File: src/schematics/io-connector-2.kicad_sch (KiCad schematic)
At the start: 1 part, among them J13 DDR4_SODIMM_Board

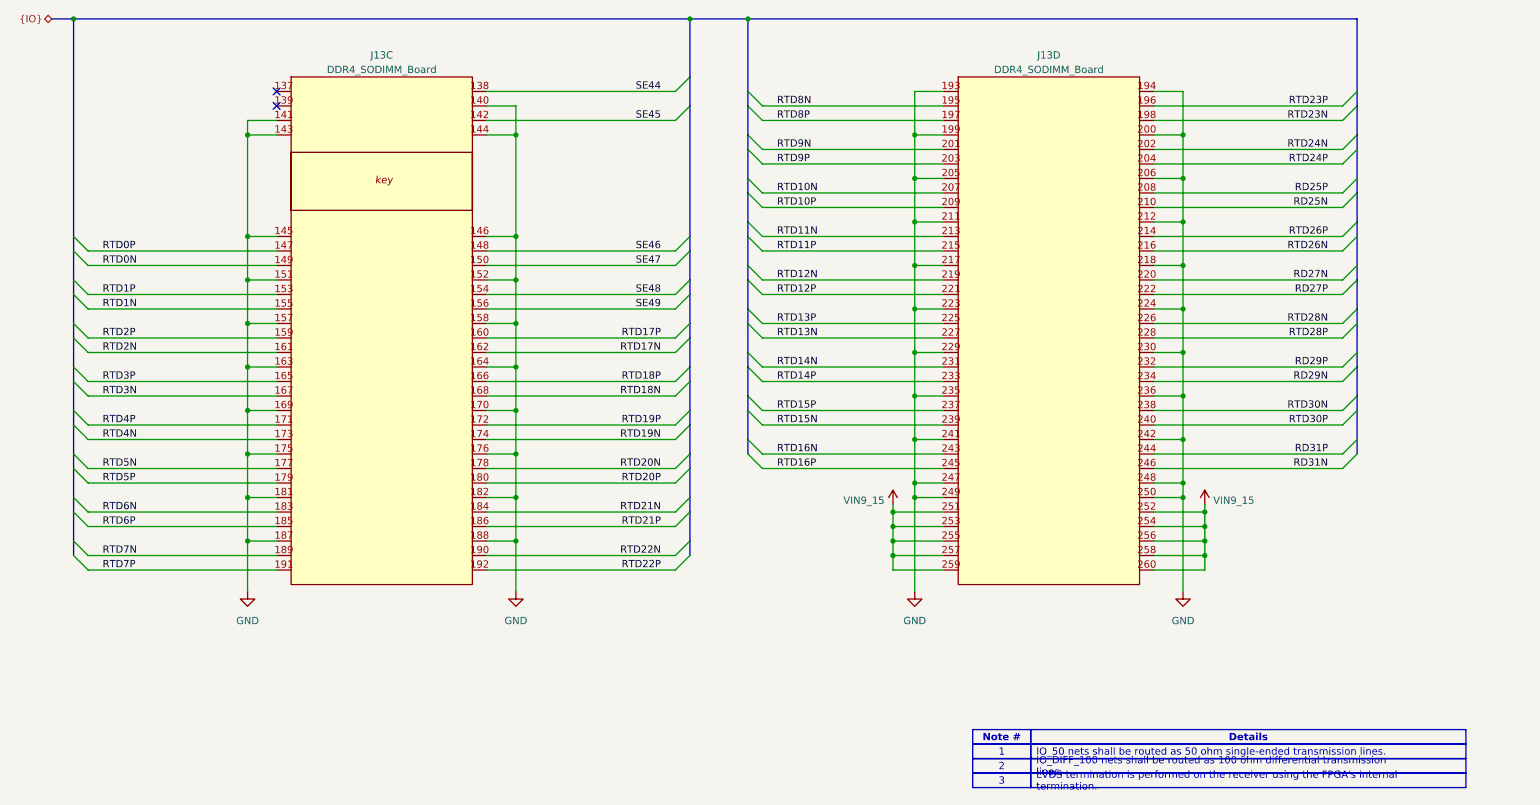
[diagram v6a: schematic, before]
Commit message: Fix diff pair skew
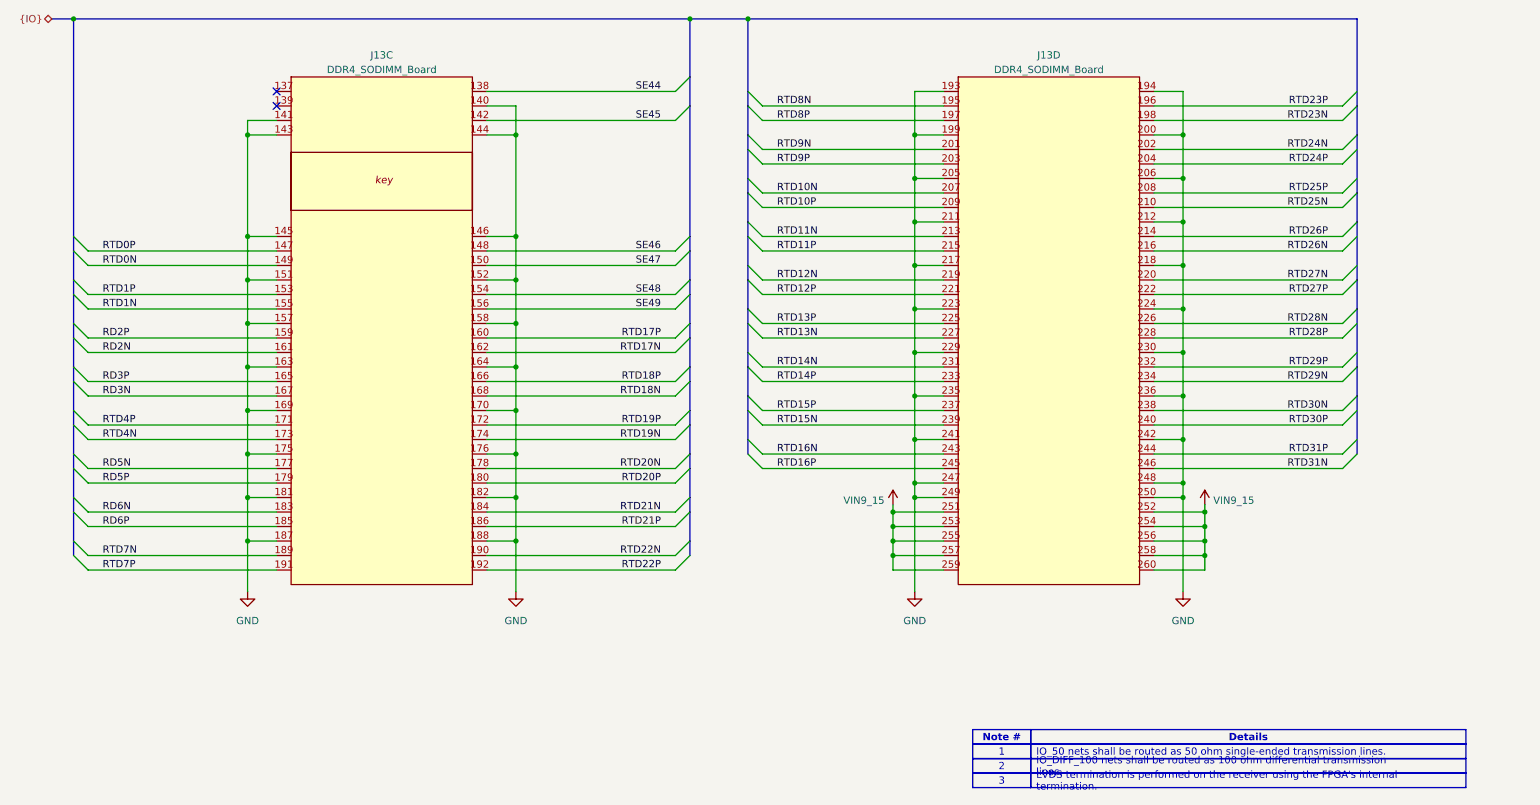
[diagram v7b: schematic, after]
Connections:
- net RD25N renamed RTD25N
- net RD25P renamed RTD25P
- net RD27N renamed RTD27N
- net RD27P renamed RTD27P
- net RD29N renamed RTD29N
- net RD29P renamed RTD29P
- net RD31N renamed RTD31N
- net RD31P renamed RTD31P
- net RTD2N renamed RD2N
- net RTD2P renamed RD2P
- net RTD3N renamed RD3N
- net RTD3P renamed RD3P
- net RTD5N renamed RD5N
- net RTD5P renamed RD5P
- net RTD6N renamed RD6N
- net RTD6P renamed RD6P
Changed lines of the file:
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@@
 		)
 	)
-	(label "RD27P"
+	(label "RTD27P"
 		(at 257.81 86.36 180)
 		(effects
@@
 		)
 	)
-	(label "RTD3P"
+	(label "RD3P"
 		(at 43.18 101.6 0)
 		(effects
@@
 		)
 	)
-	(label "RTD2P"
+	(label "RD2P"
 		(at 43.18 93.98 0)
 		(effects
@@
 		)
 	)
-	(label "RTD6P"
+	(label "RD6P"
 		(at 43.18 127 0)
 		(effects
@@
 		)
 	)
-	(label "RTD5N"
+	(label "RD5N"
 		(at 43.18 116.84 0)
 		(effects
@@
 		)
 	)
-	(label "RD29P"
+	(label "RTD29P"
 		(at 257.81 99.06 180)
 		(effects
@@
 		)
 	)
-	(label "RD29N"
+	(label "RTD29N"
 		(at 257.81 101.6 180)
 		(effects
@@
 		)
 	)
-	(label "RD31N"
+	(label "RTD31N"
 		(at 257.81 116.84 180)
 		(effects
@@
 		)
 	)
-	(label "RTD2N"
+	(label "RD2N"
 		(at 43.18 96.52 0)
 		(effects
@@
 		)
 	)
-	(label "RD25N"
+	(label "RTD25N"
 		(at 257.81 71.12 180)
 		(effects
@@
 		)
 	)
-	(label "RD27N"
+	(label "RTD27N"
 		(at 257.81 83.82 180)
 		(effects
@@
 		)
 	)
-	(label "RTD6N"
+	(label "RD6N"
 		(at 43.18 124.46 0)
 		(effects
@@
 		)
 	)
-	(label "RD31P"
+	(label "RTD31P"
 		(at 257.81 114.3 180)
 		(effects
@@
 		)
 	)
-	(label "RTD3N"
+	(label "RD3N"
 		(at 43.18 104.14 0)
 		(effects
@@
 		)
 	)
-	(label "RD25P"
+	(label "RTD25P"
 		(at 257.81 68.58 180)
 		(effects
@@
 		)
 	)
-	(label "RTD5P"
+	(label "RD5P"
 		(at 43.18 119.38 0)
 		(effects
